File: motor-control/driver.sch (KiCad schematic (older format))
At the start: 1 part

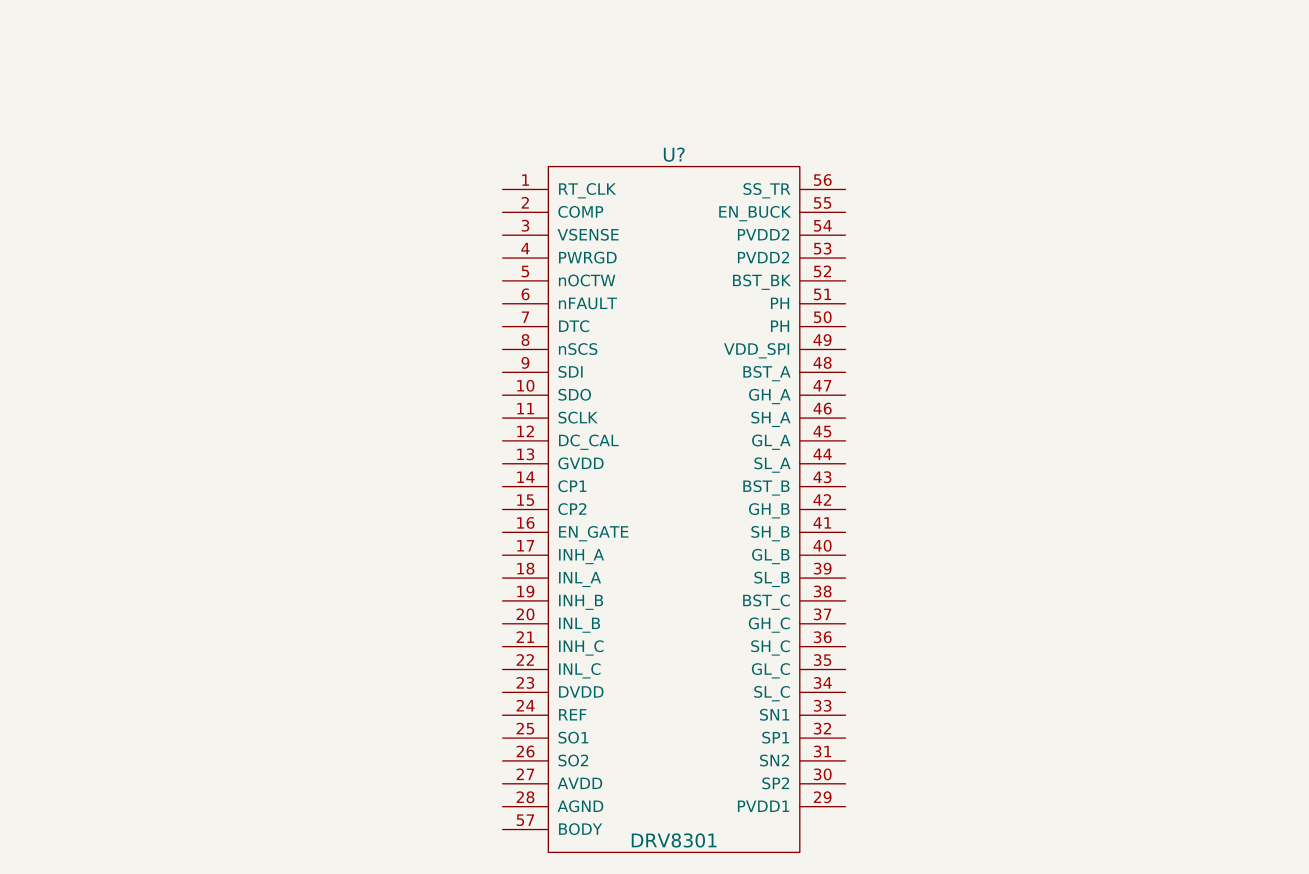
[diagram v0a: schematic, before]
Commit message: Almost finished gate driver schematic
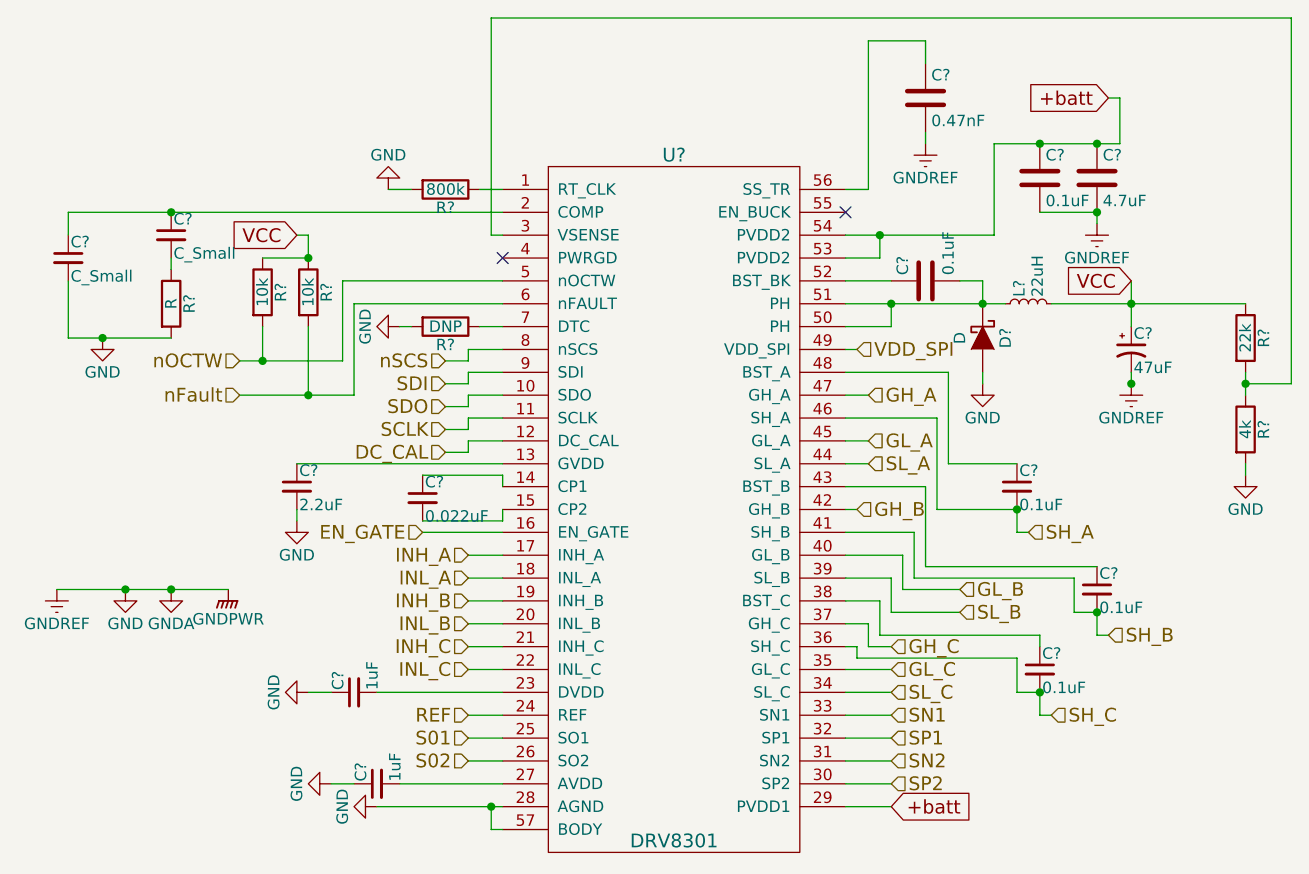
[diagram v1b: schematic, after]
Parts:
- added C?: 0.47nF, symbol C
- added C? (x2): 0.1uF, symbol C
- added C?: 4.7uF, symbol C
- added C?: 47uF, symbol CP1_Small
- added C?: 2.2uF, symbol C_Small
- added C? (x2): C_Small, symbol C_Small
- added C? (x2): 1uF, symbol C_Small
- added C?: 0.022uF, symbol C_Small
- added C? (x3): 0.1uF, symbol C_Small
- added D?: D, symbol D_Schottky
- added L?: 22uH, symbol L_Small
- added R?: R, symbol R
- added R?: 800k, symbol R
- added R? (x2): 10k, symbol R
- added R?: 22k, symbol R
- added R?: 4k, symbol R
- added R?: DNP, symbol R
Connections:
- net at U?.1 (RT_CLK): now also R?.1
- net SDO: now reaches U?.10 (SDO)
- net SCLK: now reaches U?.11 (SCLK)
- net DC_CAL: now reaches U?.12 (DC_CAL)
- net at U?.13 (GVDD): now also C?.1
- net at U?.14 (CP1): now also C?.1
- net at U?.15 (CP2): now also C?.2
- net EN_GATE: now reaches U?.16 (EN_GATE)
- net INH_A: now reaches U?.17 (INH_A)
- net INL_A: now reaches U?.18 (INL_A)
- net INH_B: now reaches U?.19 (INH_B)
- net at U?.2 (COMP): now also C?.1, C?.1
- net INL_B: now reaches U?.20 (INL_B)
- net INH_C: now reaches U?.21 (INH_C)
- net INL_C: now reaches U?.22 (INL_C)
- net at U?.23 (DVDD): now also C?.2
- net REF: now reaches U?.24 (REF)
- net S01: now reaches U?.25 (SO1)
- net S02: now reaches U?.26 (SO2)
- net at U?.27 (AVDD): now also C?.2
- net GND: now reaches U?.28 (AGND)
- net GND: now also U?.57 (BODY), C?.1, C?.1, C?.2, C?.2, C?.2, C?.2, C?.2, C?.2, D?.2 (A), R?.2, R?.2, R?.2, R?.2
- net +batt: now reaches U?.29 (PVDD1)
- net +batt: now also U?.53 (PVDD2), U?.54 (PVDD2), C?.1, C?.1
- net at U?.3 (VSENSE): now also R?.1, R?.2
- net SP2: now reaches U?.30 (SP2)
- net SN2: now reaches U?.31 (SN2)
- net SP1: now reaches U?.32 (SP1)
- net SN1: now reaches U?.33 (SN1)
- net SL_C: now reaches U?.34 (SL_C)
- net GL_C: now reaches U?.35 (GL_C)
- net SH_C: now reaches U?.36 (SH_C)
- net SH_C: now also C?.2
- net GH_C: now reaches U?.37 (GH_C)
- net at U?.38 (BST_C): now also C?.1
- net SL_B: now reaches U?.39 (SL_B)
- net GL_B: now reaches U?.40 (GL_B)
- net SH_B: now reaches U?.41 (SH_B)
- net SH_B: now also C?.2
- net GH_B: now reaches U?.42 (GH_B)
- net at U?.43 (BST_B): now also C?.1
- net SL_A: now reaches U?.44 (SL_A)
- net GL_A: now reaches U?.45 (GL_A)
- net SH_A: now reaches U?.46 (SH_A)
- net SH_A: now also C?.2
- net GH_A: now reaches U?.47 (GH_A)
- net at U?.48 (BST_A): now also C?.1
- net VDD_SPI: now reaches U?.49 (VDD_SPI)
- net nOCTW: now reaches U?.5 (nOCTW)
- net nOCTW: now also R?.2
- net at U?.50 (PH): now also U?.51 (PH), C?.2, D?.1 (K), L?.1
- net at U?.52 (BST_BK): now also C?.1
- net at U?.56 (SS_TR): now also C?.1
- net nFault: now reaches U?.6 (nFAULT)
- net nFault: now also R?.2
- net at U?.7 (DTC): now also R?.1
- net nSCS: now reaches U?.8 (nSCS)
- net SDI: now reaches U?.9 (SDI)
- new net: C?.2, R?.1
- new net VCC: C?.1, L?.2, R?.1, R?.1, R?.1
- no-connect marks 0 -> 2
